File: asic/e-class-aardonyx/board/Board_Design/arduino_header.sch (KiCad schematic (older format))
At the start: 32 parts, among them J10 Conn_1x6_F, J11 Conn_1x6_F, J12 Conn_1x3_M, J13 Conn_1x8_F, J14 Conn_1x6_F, J15 Conn_1x10, J16 Conn_1x8_F, J19 Conn_1x3_M, J7 Conn_1x4, J8 Conn_1x3_M, J9 Conn_1x8, U5 CAT24M01WI-GT3, U6 IS25LP256x-xM, U7 ADC108S102CIMTX, U8 LSF0108PWR, U9 LSF0108PWR

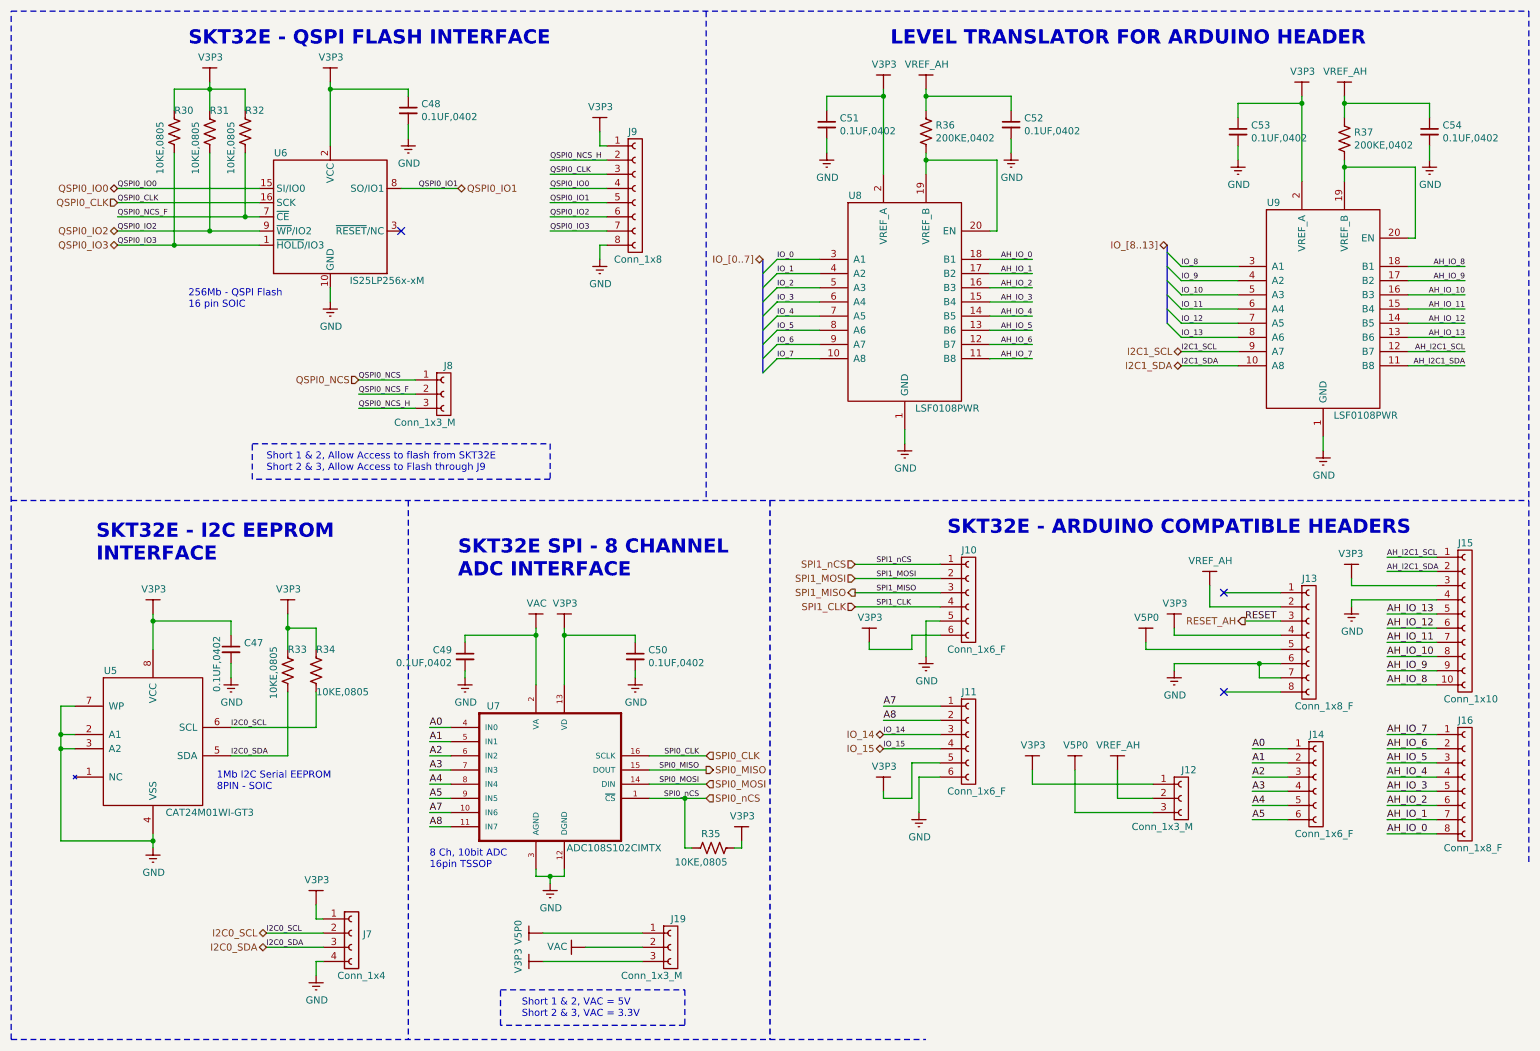
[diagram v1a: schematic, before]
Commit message: update component palcement comment by kottee
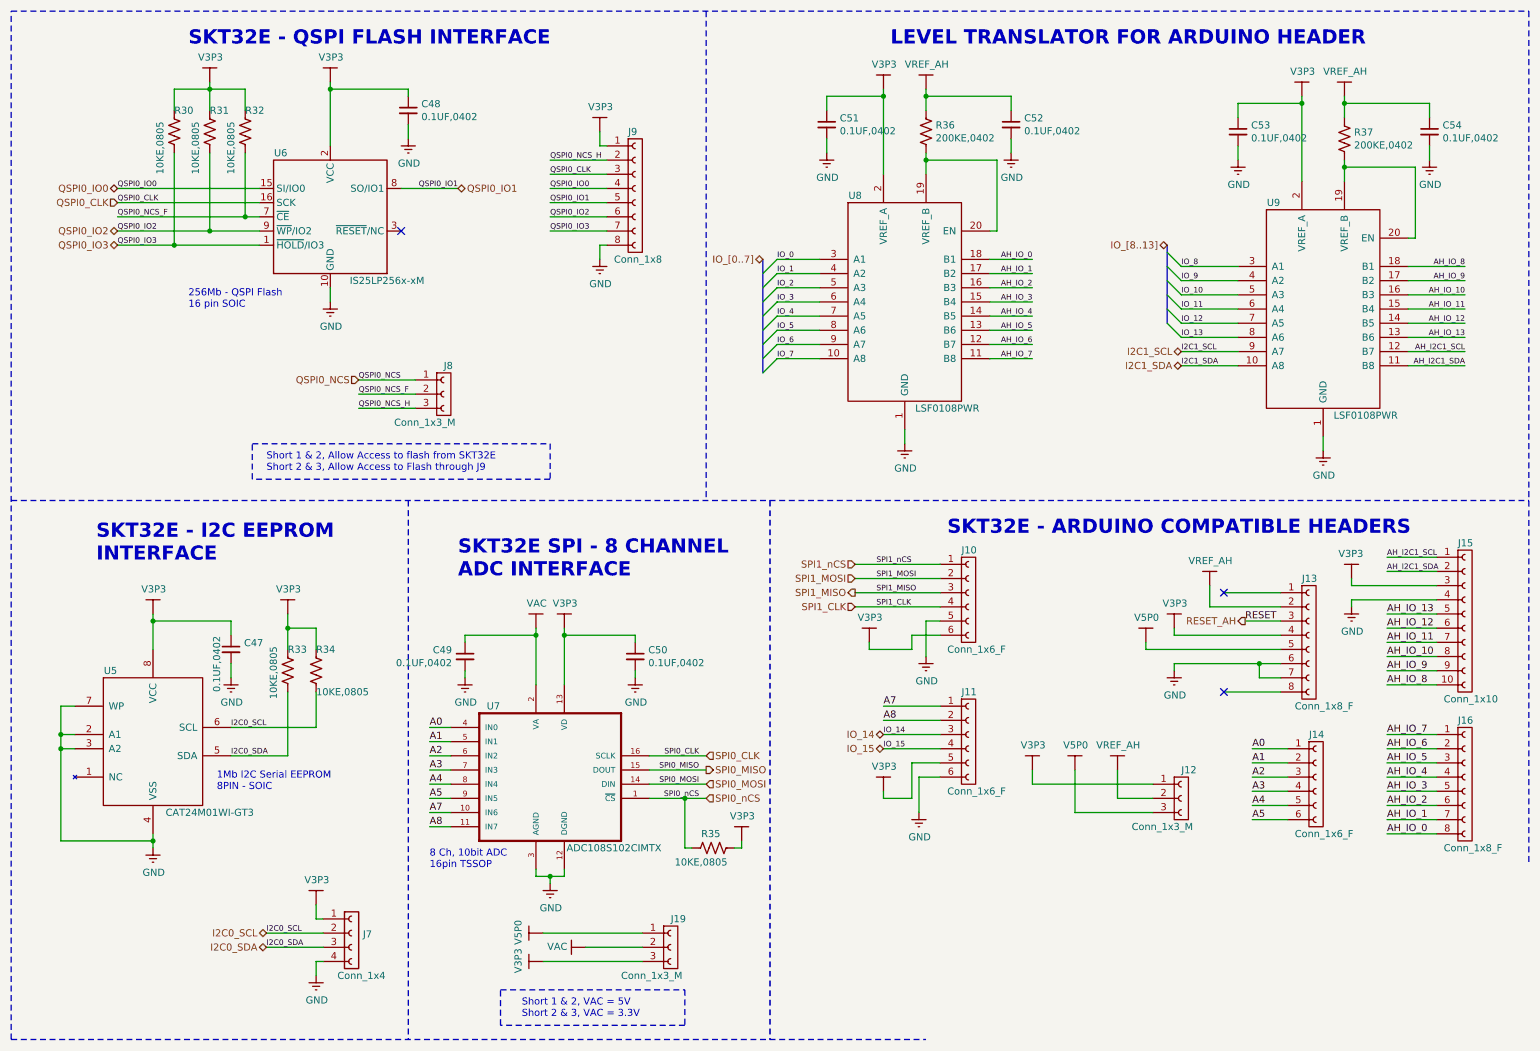
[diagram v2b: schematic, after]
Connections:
- net VAC: no longer names the net of C49.1, U7.2 (VA)
- net VAC: no longer J19.2 (Pin_2)
- removed net VREF_AH: C52.1, C54.1, J12.2 (Pin_2), J13.2 (Pin_2), R36.1, R37.1
- new net: C52.1, R36.1
- new net: C54.1, R37.1
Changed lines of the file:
@@
 $EndComp
 $Comp
-L Aardonyx-rescue:VREF_AH-aardonyx #PWR076
+L Aardonyx-rescue:VREF_AH-aardonyx-Aardonyx-rescue #PWR076
 U 1 1 5DCD16BF
 P 6950 1050
@@
 $EndComp
 $Comp
-L Aardonyx-rescue:VREF_AH-aardonyx #PWR089
+L Aardonyx-rescue:VREF_AH-aardonyx-Aardonyx-rescue #PWR089
 U 1 1 5DCDE768
 P 9900 1100
@@
 $EndComp
 $Comp
-L Aardonyx-rescue:VREF_AH-aardonyx #PWR081
+L Aardonyx-rescue:VREF_AH-aardonyx-Aardonyx-rescue #PWR081
 U 1 1 5DCEB777
 P 8300 5850
@@
 	9950 4550 10550 4550
 $Comp
-L Aardonyx-rescue:VREF_AH-aardonyx #PWR085
+L Aardonyx-rescue:VREF_AH-aardonyx-Aardonyx-rescue #PWR085
 U 1 1 5DE472F1
 P 8950 4550
@@
 8 Ch, 10bit ADC\n16pin TSSOP
 $Comp
-L Aardonyx-rescue:VAC #PWR0156
+L Aardonyx-rescue:VAC-Aardonyx-rescue #PWR0156
 U 1 1 5F0884B4
 P 4200 4850
@@
 	4250 7200 4950 7200
 $Comp
-L Aardonyx-rescue:VAC #PWR0159
+L Aardonyx-rescue:VAC-Aardonyx-rescue #PWR0159
 U 1 1 5F100A5C
 P 4550 7100

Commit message: add bom
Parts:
- J10, J11, J14: Manufactured Part Number 75915-306LF -> 75915-306LF
- J13, J16: Manufactured Part Number 68685-308LF -> 68685-308LF
- J9: Digikey PartNumber 609-3264-ND -> 609-3264-ND
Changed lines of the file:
@@
 F 4 "CONN RCPT 6POS 0.1 GOLD PCB" H 9700 5900 50  0001 C CNN "Description"
 F 5 "609-3558-ND" H 9700 5900 50  0001 C CNN "Digikey PartNumber"
-F 6 "	75915-306LF" H 9700 5900 50  0001 C CNN "Manufactured Part Number"
+F 6 "75915-306LF" H 9700 5900 50  0001 C CNN "Manufactured Part Number"
 F 7 "Amphenol ICC (FCI)" H 9700 5900 50  0001 C CNN "Maufaturer"
 	1    9700 5900
@@
 F 4 "CONN RCPT 8POS 0.1 GOLD PCB" H 10750 5900 50  0001 C CNN "Description"
 F 5 "609-3589-ND" H 10750 5900 50  0001 C CNN "Digikey PartNumber"
-F 6 "	68685-308LF" H 10750 5900 50  0001 C CNN "Manufactured Part Number"
+F 6 "68685-308LF" H 10750 5900 50  0001 C CNN "Manufactured Part Number"
 F 7 "Amphenol ICC (FCI)" H 10750 5900 50  0001 C CNN "Maufaturer"
 	1    10750 5900
@@
 F 4 "CONN RCPT 8POS 0.1 GOLD PCB" H 9650 4900 50  0001 C CNN "Description"
 F 5 "609-3589-ND" H 9650 4900 50  0001 C CNN "Digikey PartNumber"
-F 6 "	68685-308LF" H 9650 4900 50  0001 C CNN "Manufactured Part Number"
+F 6 "68685-308LF" H 9650 4900 50  0001 C CNN "Manufactured Part Number"
 F 7 "Amphenol ICC (FCI)" H 9650 4900 50  0001 C CNN "Maufaturer"
 F 8 "609-3589-ND" H 9650 4900 50  0001 C CNN "Field4"
@@
 F 4 "CONN RCPT 6POS 0.1 GOLD PCB" H 7250 4600 50  0001 C CNN "Description"
 F 5 "609-3558-ND" H 7250 4600 50  0001 C CNN "Digikey PartNumber"
-F 6 "	75915-306LF" H 7250 4600 50  0001 C CNN "Manufactured Part Number"
+F 6 "75915-306LF" H 7250 4600 50  0001 C CNN "Manufactured Part Number"
 F 7 "Amphenol ICC (FCI)" H 7250 4600 50  0001 C CNN "Maufaturer"
 	1    7250 4600
@@
 F 3 "https://www.digikey.com/products/en?keywords=68000-408HLF" H 4900 1750 50  0001 C CNN
 F 4 "CONN HEADER VERT 8POS 2.54MM" H 4900 1750 50  0001 C CNN "Description"
-F 5 "	609-3264-ND" H 4900 1750 50  0001 C CNN "Digikey PartNumber"
+F 5 "609-3264-ND" H 4900 1750 50  0001 C CNN "Digikey PartNumber"
 F 6 "68000-408HLF" H 4900 1750 50  0001 C CNN "Manufactured Part Number"
 F 7 "Amphenol ICC (FCI)" H 4900 1750 50  0001 C CNN "Maufaturer"
@@
 F 4 "CONN RCPT 6POS 0.1 GOLD PCB" H 7250 5600 50  0001 C CNN "Description"
 F 5 "609-3558-ND" H 7250 5600 50  0001 C CNN "Digikey PartNumber"
-F 6 "	75915-306LF" H 7250 5600 50  0001 C CNN "Manufactured Part Number"
+F 6 "75915-306LF" H 7250 5600 50  0001 C CNN "Manufactured Part Number"
 F 7 "Amphenol ICC (FCI)" H 7250 5600 50  0001 C CNN "Maufaturer"
 	1    7250 5600

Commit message: Updated few components
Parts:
- U5: Digikey PartNumber CAT24M01WI-GT3OSCT-ND -> CAT24M01XI-T2OSCT-ND; Manufactured Part Number CAT24M01WI-GT3 -> CAT24M01XI-T2
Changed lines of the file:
@@
 EESchema Schematic File Version 4
-EELAYER 30 0
+LIBS:Aardonyx-cache
+EELAYER 29 0
 EELAYER END
 $Descr A4 11693 8268
@@
 F 3 "https://www.digikey.in/product-detail/en/on-semiconductor/CAT24M01WI-GT3/CAT24M01WI-GT3OSCT-ND/2698362" H 1500 5650 50  0001 C CNN
 F 4 "IC EEPROM 1M I2C 1MHZ 8SOIC" H 1500 5650 50  0001 C CNN "Description"
-F 5 "CAT24M01WI-GT3OSCT-ND" H 1500 5650 50  0001 C CNN "Digikey PartNumber"
-F 6 "CAT24M01WI-GT3" H 1500 5650 50  0001 C CNN "Manufactured Part Number"
+F 5 "CAT24M01XI-T2OSCT-ND" H 1500 5650 50  0001 C CNN "Digikey PartNumber"
+F 6 "CAT24M01XI-T2" H 1500 5650 50  0001 C CNN "Manufactured Part Number"
 F 7 "ON Semiconductor" H 1500 5650 50  0001 C CNN "Maufaturer"
 	1    1500 5650

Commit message: Updating BOM
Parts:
- U7: value ADC108S102CIMTX -> ADC128S102CIMTX/NOPB; Description ADC108S102CIMTX/NOPB -> IC ADC 12BIT SAR 16TSSOP; Digikey PartNumber 296-43835-1-ND -> 296-41184-1-ND; Manufactured Part Number ADC108S102CIMTX/NOPB -> ADC128S102CIMTX/NOPB
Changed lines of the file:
@@
 P 4300 5900
 F 0 "U7" H 3900 6400 50  0000 C CNN
-F 1 "ADC108S102CIMTX" H 4750 5400 50  0000 C CNN
+F 1 "ADC128S102CIMTX/NOPB" H 4750 5400 50  0000 C CNN
 F 2 "Package_SO:TSSOP-16_4.4x5mm_P0.65mm" H 4300 5900 50  0001 L BNN
-F 3 "https://www.digikey.in/product-detail/en/texas-instruments/ADC108S102CIMTX-NOPB/296-43835-1-ND/5875706" H 4300 5900 50  0001 L BNN
-F 4 "ADC108S102CIMTX/NOPB" H 4300 5900 50  0001 C CNN "Description"
-F 5 "296-43835-1-ND" H 4300 5900 50  0001 C CNN "Digikey PartNumber"
-F 6 "ADC108S102CIMTX/NOPB" H 4300 5900 50  0001 C CNN "Manufactured Part Number"
+F 3 "https://www.digikey.in/product-detail/en/texas-instruments/ADC128S102CIMTX-NOPB/296-41184-1-ND/5222639" H 4300 5900 50  0001 L BNN
+F 4 "IC ADC 12BIT SAR 16TSSOP" H 4300 5900 50  0001 C CNN "Description"
+F 5 "296-41184-1-ND" H 4300 5900 50  0001 C CNN "Digikey PartNumber"
+F 6 "ADC128S102CIMTX/NOPB" H 4300 5900 50  0001 C CNN "Manufactured Part Number"
 F 7 "Texas Instruments" H 4300 5900 50  0001 C CNN "Maufaturer"
 	1    4300 5900

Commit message: update footprint & bom
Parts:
- R36, R37: Description RES 200K OHM 0.1% 1/16W 0402 -> RES 200K OHM 0.1% 1/16W 0402
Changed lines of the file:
@@
 EESchema Schematic File Version 4
-LIBS:Aardonyx-cache
-EELAYER 29 0
+EELAYER 30 0
 EELAYER END
 $Descr A4 11693 8268
@@
 F 2 "Resistor_SMD:R_0402_1005Metric" V 6990 1340 50  0001 C CNN
 F 3 "https://www.digikey.com/product-detail/en/koa-speer-electronics-inc/RN73H1ETTP2003B25/2019-RN73H1ETTP2003B25CT-ND/9916930" H 6950 1350 50  0001 C CNN
-F 4 " RES 200K OHM 0.1% 1/16W 0402 " H 6950 1350 50  0001 C CNN "Description"
+F 4 "RES 200K OHM 0.1% 1/16W 0402 " H 6950 1350 50  0001 C CNN "Description"
 F 5 "2019-RN73H1ETTP2003B25CT-ND " H 6950 1350 50  0001 C CNN "Digikey PartNumber"
 F 6 "RN73H1ETTP2003B25" H 6950 1350 50  0001 C CNN "Manufactured Part Number"
@@
 F 2 "Resistor_SMD:R_0402_1005Metric" V 9940 1390 50  0001 C CNN
 F 3 "https://www.digikey.com/product-detail/en/koa-speer-electronics-inc/RN73H1ETTP2003B25/2019-RN73H1ETTP2003B25CT-ND/9916930" H 9900 1400 50  0001 C CNN
-F 4 " RES 200K OHM 0.1% 1/16W 0402 " H 9900 1400 50  0001 C CNN "Description"
+F 4 "RES 200K OHM 0.1% 1/16W 0402 " H 9900 1400 50  0001 C CNN "Description"
 F 5 "2019-RN73H1ETTP2003B25CT-ND " H 9900 1400 50  0001 C CNN "Digikey PartNumber"
 F 6 "RN73H1ETTP2003B25" H 9900 1400 50  0001 C CNN "Manufactured Part Number"

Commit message: Added few components
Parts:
- R30, R31, R32, R33, R34, R35: value 10KE,0805 -> 10KE,0402; footprint Resistor_SMD:R_0805_2012Metric -> Resistor_SMD:R_0402_1005Metric; Description RES SMD 10K OHM 1% 1/8W 0805 -> RES 10K OHM 5% 1/8W 0402; Digikey PartNumber 311-10.0KCRCT-ND -> 2019-SG73S1ETTP103JCT-ND; Manufactured Part Number RC0805FR-0710KL -> SG73S1ETTP103J; Maufaturer Yageo -> KOA Speer Electronics, Inc.
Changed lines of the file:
@@
 P 2150 1350
 F 0 "R32" H 2150 1500 50  0000 L CNN
-F 1 "10KE,0805" V 2050 1050 50  0000 L CNN
-F 2 "Resistor_SMD:R_0805_2012Metric" V 2190 1340 50  0001 C CNN
-F 3 "https://www.digikey.in/product-detail/en/yageo/RC0805FR-0710KL/311-10-0KCRCT-ND/730482" H 2150 1350 50  0001 C CNN
-F 4 "RES SMD 10K OHM 1% 1/8W 0805" H 2150 1350 50  0001 C CNN "Description"
-F 5 "311-10.0KCRCT-ND" H 2150 1350 50  0001 C CNN "Digikey PartNumber"
-F 6 "RC0805FR-0710KL" H 2150 1350 50  0001 C CNN "Manufactured Part Number"
-F 7 "Yageo" H 2150 1350 50  0001 C CNN "Maufaturer"
+F 1 "10KE,0402" V 2050 1050 50  0000 L CNN
+F 2 "Resistor_SMD:R_0402_1005Metric" V 2190 1340 50  0001 C CNN
+F 3 "https://www.digikey.in/product-detail/en/koa-speer-electronics-inc/SG73S1ETTP103J/2019-SG73S1ETTP103JCT-ND/10280218" H 2150 1350 50  0001 C CNN
+F 4 "RES 10K OHM 5% 1/8W 0402" H 2150 1350 50  0001 C CNN "Description"
+F 5 "2019-SG73S1ETTP103JCT-ND" H 2150 1350 50  0001 C CNN "Digikey PartNumber"
+F 6 "SG73S1ETTP103J" H 2150 1350 50  0001 C CNN "Manufactured Part Number"
+F 7 "KOA Speer Electronics, Inc." H 2150 1350 50  0001 C CNN "Maufaturer"
 	1    2150 1350
 	1    0    0    -1
@@
 P 1650 1350
 F 0 "R30" H 1650 1500 50  0000 L CNN
-F 1 "10KE,0805" V 1550 1050 50  0000 L CNN
-F 2 "Resistor_SMD:R_0805_2012Metric" V 1690 1340 50  0001 C CNN
-F 3 "https://www.digikey.in/product-detail/en/yageo/RC0805FR-0710KL/311-10-0KCRCT-ND/730482" H 1650 1350 50  0001 C CNN
-F 4 "RES SMD 10K OHM 1% 1/8W 0805" H 1650 1350 50  0001 C CNN "Description"
-F 5 "311-10.0KCRCT-ND" H 1650 1350 50  0001 C CNN "Digikey PartNumber"
-F 6 "RC0805FR-0710KL" H 1650 1350 50  0001 C CNN "Manufactured Part Number"
-F 7 "Yageo" H 1650 1350 50  0001 C CNN "Maufaturer"
+F 1 "10KE,0402" V 1550 1050 50  0000 L CNN
+F 2 "Resistor_SMD:R_0402_1005Metric" V 1690 1340 50  0001 C CNN
+F 3 "https://www.digikey.in/product-detail/en/koa-speer-electronics-inc/SG73S1ETTP103J/2019-SG73S1ETTP103JCT-ND/10280218" H 1650 1350 50  0001 C CNN
+F 4 "RES 10K OHM 5% 1/8W 0402" H 1650 1350 50  0001 C CNN "Description"
+F 5 "2019-SG73S1ETTP103JCT-ND" H 1650 1350 50  0001 C CNN "Digikey PartNumber"
+F 6 "SG73S1ETTP103J" H 1650 1350 50  0001 C CNN "Manufactured Part Number"
+F 7 "KOA Speer Electronics, Inc." H 1650 1350 50  0001 C CNN "Maufaturer"
 	1    1650 1350
 	1    0    0    -1
@@
 P 1900 1350
 F 0 "R31" H 1900 1500 50  0000 L CNN
-F 1 "10KE,0805" V 1800 1050 50  0000 L CNN
-F 2 "Resistor_SMD:R_0805_2012Metric" V 1940 1340 50  0001 C CNN
-F 3 "https://www.digikey.in/product-detail/en/yageo/RC0805FR-0710KL/311-10-0KCRCT-ND/730482" H 1900 1350 50  0001 C CNN
-F 4 "RES SMD 10K OHM 1% 1/8W 0805" H 1900 1350 50  0001 C CNN "Description"
-F 5 "311-10.0KCRCT-ND" H 1900 1350 50  0001 C CNN "Digikey PartNumber"
-F 6 "RC0805FR-0710KL" H 1900 1350 50  0001 C CNN "Manufactured Part Number"
-F 7 "Yageo" H 1900 1350 50  0001 C CNN "Maufaturer"
+F 1 "10KE,0402" V 1800 1050 50  0000 L CNN
+F 2 "Resistor_SMD:R_0402_1005Metric" V 1940 1340 50  0001 C CNN
+F 3 "https://www.digikey.in/product-detail/en/koa-speer-electronics-inc/SG73S1ETTP103J/2019-SG73S1ETTP103JCT-ND/10280218" H 1900 1350 50  0001 C CNN
+F 4 "RES 10K OHM 5% 1/8W 0402" H 1900 1350 50  0001 C CNN "Description"
+F 5 "2019-SG73S1ETTP103JCT-ND" H 1900 1350 50  0001 C CNN "Digikey PartNumber"
+F 6 "SG73S1ETTP103J" H 1900 1350 50  0001 C CNN "Manufactured Part Number"
+F 7 "KOA Speer Electronics, Inc." H 1900 1350 50  0001 C CNN "Maufaturer"
 	1    1900 1350
 	1    0    0    -1
@@
 P 2450 5150
 F 0 "R33" H 2450 5300 50  0000 L CNN
-F 1 "10KE,0805" V 2350 4950 50  0000 L CNN
-F 2 "Resistor_SMD:R_0805_2012Metric" V 2490 5140 50  0001 C CNN
-F 3 "https://www.digikey.in/product-detail/en/yageo/RC0805FR-0710KL/311-10-0KCRCT-ND/730482" H 2450 5150 50  0001 C CNN
-F 4 "RES SMD 10K OHM 1% 1/8W 0805" H 2450 5150 50  0001 C CNN "Description"
-F 5 "311-10.0KCRCT-ND" H 2450 5150 50  0001 C CNN "Digikey PartNumber"
-F 6 "RC0805FR-0710KL" H 2450 5150 50  0001 C CNN "Manufactured Part Number"
-F 7 "Yageo" H 2450 5150 50  0001 C CNN "Maufaturer"
+F 1 "10KE,0402" V 2350 4950 50  0000 L CNN
+F 2 "Resistor_SMD:R_0402_1005Metric" V 2490 5140 50  0001 C CNN
+F 3 "https://www.digikey.in/product-detail/en/koa-speer-electronics-inc/SG73S1ETTP103J/2019-SG73S1ETTP103JCT-ND/10280218" H 2450 5150 50  0001 C CNN
+F 4 "RES 10K OHM 5% 1/8W 0402" H 2450 5150 50  0001 C CNN "Description"
+F 5 "2019-SG73S1ETTP103JCT-ND" H 2450 5150 50  0001 C CNN "Digikey PartNumber"
+F 6 "SG73S1ETTP103J" H 2450 5150 50  0001 C CNN "Manufactured Part Number"
+F 7 "KOA Speer Electronics, Inc." H 2450 5150 50  0001 C CNN "Maufaturer"
 	1    2450 5150
 	1    0    0    -1
@@
 P 2650 5150
 F 0 "R34" H 2650 5300 50  0000 L CNN
-F 1 "10KE,0805" H 2650 5000 50  0000 L CNN
-F 2 "Resistor_SMD:R_0805_2012Metric" V 2690 5140 50  0001 C CNN
-F 3 "https://www.digikey.in/product-detail/en/yageo/RC0805FR-0710KL/311-10-0KCRCT-ND/730482" H 2650 5150 50  0001 C CNN
-F 4 "RES SMD 10K OHM 1% 1/8W 0805" H 2650 5150 50  0001 C CNN "Description"
-F 5 "311-10.0KCRCT-ND" H 2650 5150 50  0001 C CNN "Digikey PartNumber"
-F 6 "RC0805FR-0710KL" H 2650 5150 50  0001 C CNN "Manufactured Part Number"
-F 7 "Yageo" H 2650 5150 50  0001 C CNN "Maufaturer"
+F 1 "10KE,0402" H 2650 5000 50  0000 L CNN
+F 2 "Resistor_SMD:R_0402_1005Metric" V 2690 5140 50  0001 C CNN
+F 3 "https://www.digikey.in/product-detail/en/koa-speer-electronics-inc/SG73S1ETTP103J/2019-SG73S1ETTP103JCT-ND/10280218" H 2650 5150 50  0001 C CNN
+F 4 "RES 10K OHM 5% 1/8W 0402" H 2650 5150 50  0001 C CNN "Description"
+F 5 "2019-SG73S1ETTP103JCT-ND" H 2650 5150 50  0001 C CNN "Digikey PartNumber"
+F 6 "SG73S1ETTP103J" H 2650 5150 50  0001 C CNN "Manufactured Part Number"
+F 7 "KOA Speer Electronics, Inc." H 2650 5150 50  0001 C CNN "Maufaturer"
 	1    2650 5150
 	1    0    0    -1
@@
 P 5450 6400
 F 0 "R35" V 5550 6350 50  0000 L CNN
-F 1 "10KE,0805" V 5350 6300 50  0000 L CNN
-F 2 "Resistor_SMD:R_0805_2012Metric" V 5490 6390 50  0001 C CNN
-F 3 "https://www.digikey.in/product-detail/en/yageo/RC0805FR-0710KL/311-10-0KCRCT-ND/730482" H 5450 6400 50  0001 C CNN
-F 4 "RES SMD 10K OHM 1% 1/8W 0805" H 5450 6400 50  0001 C CNN "Description"
-F 5 "311-10.0KCRCT-ND" H 5450 6400 50  0001 C CNN "Digikey PartNumber"
-F 6 "RC0805FR-0710KL" H 5450 6400 50  0001 C CNN "Manufactured Part Number"
-F 7 "Yageo" H 5450 6400 50  0001 C CNN "Maufaturer"
+F 1 "10KE,0402" V 5350 6300 50  0000 L CNN
+F 2 "Resistor_SMD:R_0402_1005Metric" V 5490 6390 50  0001 C CNN
+F 3 "https://www.digikey.in/product-detail/en/koa-speer-electronics-inc/SG73S1ETTP103J/2019-SG73S1ETTP103JCT-ND/10280218" H 5450 6400 50  0001 C CNN
+F 4 "RES 10K OHM 5% 1/8W 0402" H 5450 6400 50  0001 C CNN "Description"
+F 5 "2019-SG73S1ETTP103JCT-ND" H 5450 6400 50  0001 C CNN "Digikey PartNumber"
+F 6 "SG73S1ETTP103J" H 5450 6400 50  0001 C CNN "Manufactured Part Number"
+F 7 "KOA Speer Electronics, Inc." H 5450 6400 50  0001 C CNN "Maufaturer"
 	1    5450 6400
 	0    -1   -1   0
